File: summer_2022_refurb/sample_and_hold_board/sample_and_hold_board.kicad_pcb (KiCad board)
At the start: 2 copper layers, 40.6 x 203.2 mm, 77 parts, among them J1 VCO_port, J2 VCF_port, J3 ribbon_port, J4 power_entry, Q1 MMBT3904, Q2 2N3904, Q3 MMBT3904, SW1 SW_SPDT, U1 TL072, U2 TL072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

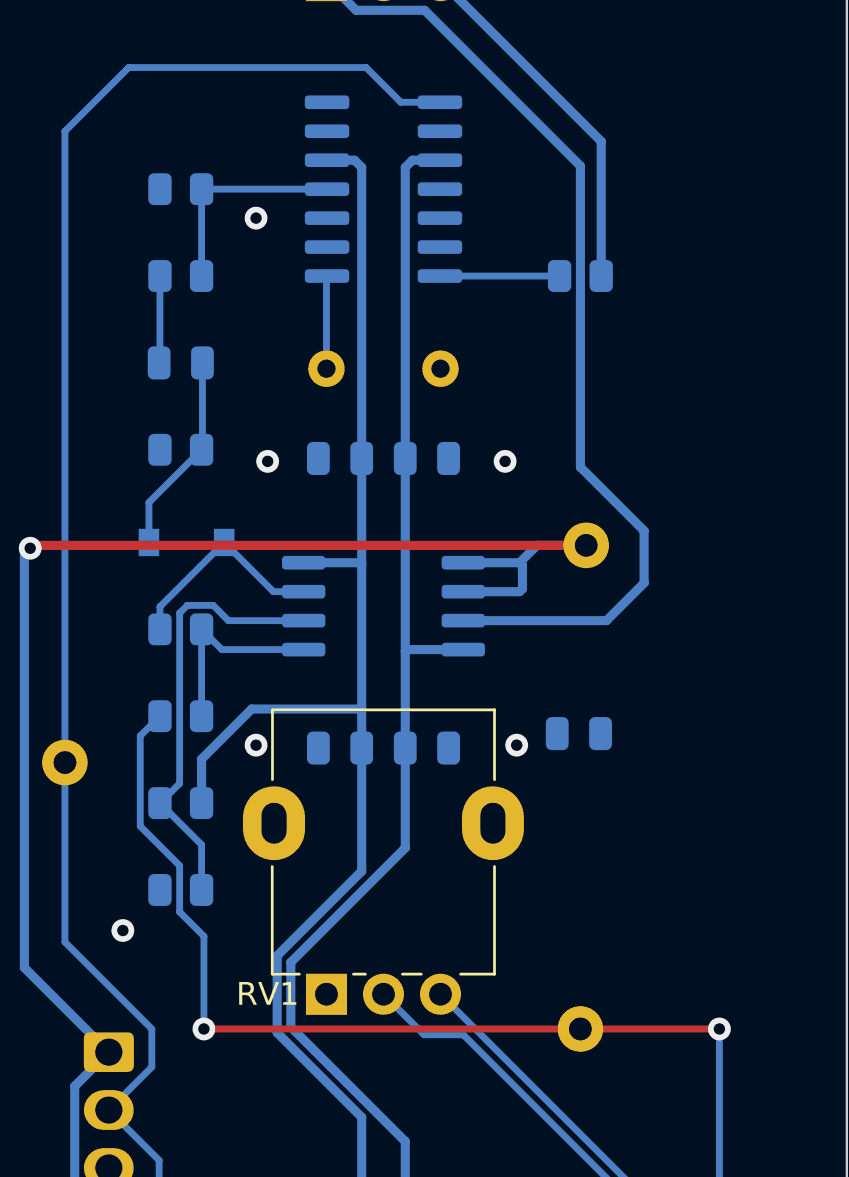
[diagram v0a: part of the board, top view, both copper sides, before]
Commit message: Change glide cap footprint, tweak silkscreen
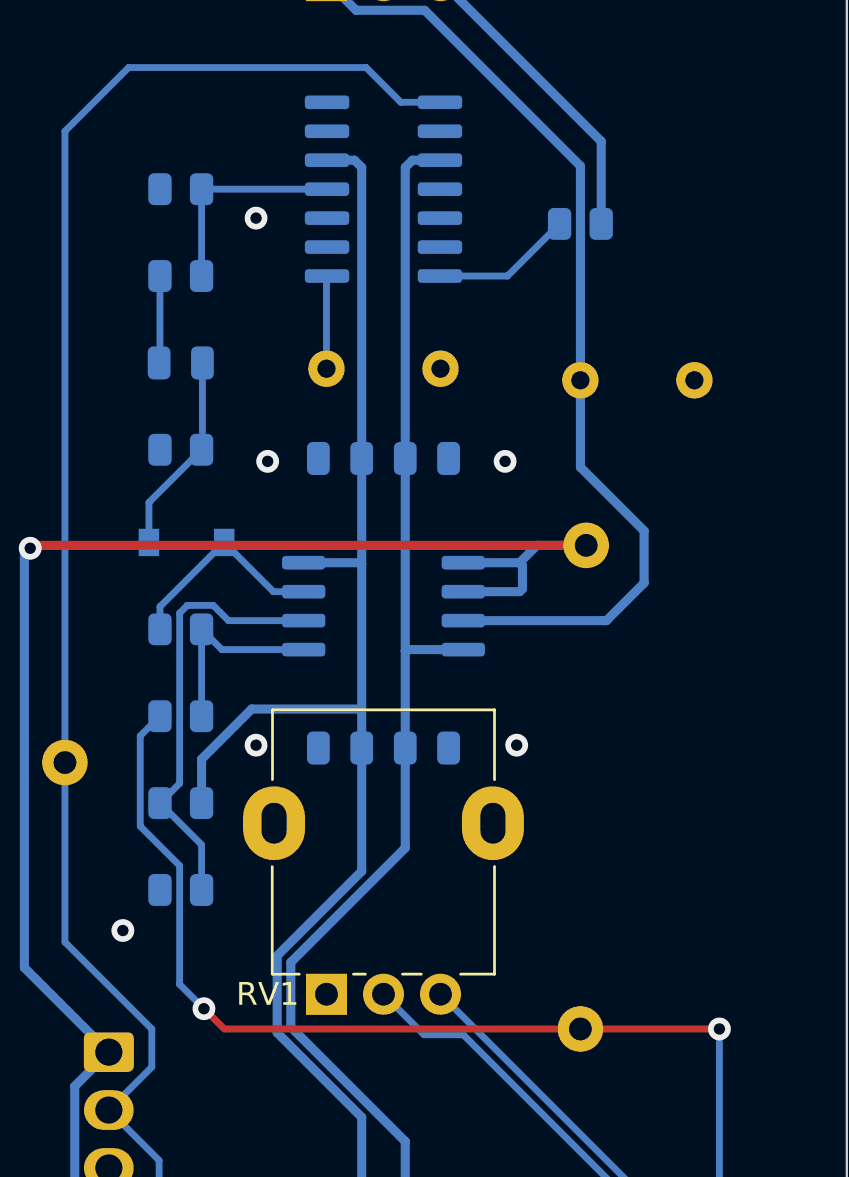
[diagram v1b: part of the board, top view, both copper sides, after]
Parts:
- C13: value C -> 470n; footprint Capacitor_SMD:C_0805_2012Metric -> Capacitor_THT:C_Rect_L7.2mm_W5.5mm_P5.00mm_FKS2_FKP2_MKS2_MKP2
- moved C13 15.5 mm to (128.0, 49.3)
- moved R24 2.29 mm to (128.0, 42.4)
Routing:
- net Net-(R24-Pad2): track 18.4 -> 16.1 mm
- net Net-(R24-Pad1): track 5.25 -> 6.20 mm
- net /sample_and_hold/TRIGGER_IN: track 111.3 -> 110.8 mm
